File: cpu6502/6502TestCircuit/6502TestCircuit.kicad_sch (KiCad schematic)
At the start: 15 parts, among them J1 Power, J2 Power, J5 Ext RST, SW1 Reset, U6 L7805, U9 DS1813

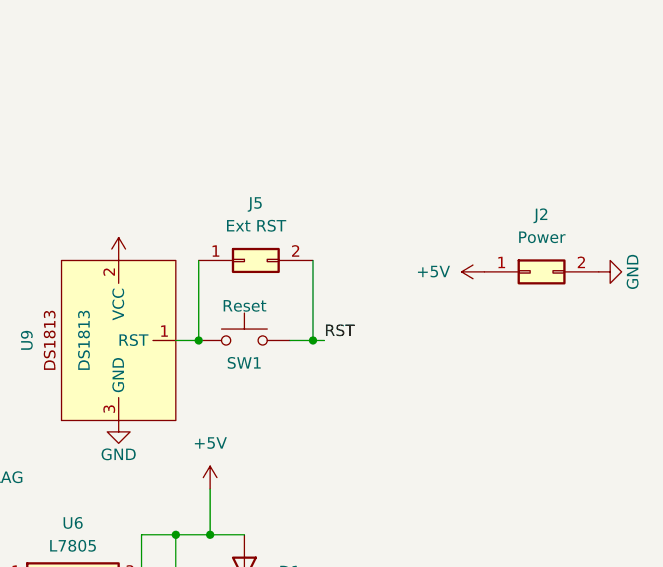
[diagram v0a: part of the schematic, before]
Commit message: PCB: Add RS232 RCV LED, get pours connected, CODE: checkpoint
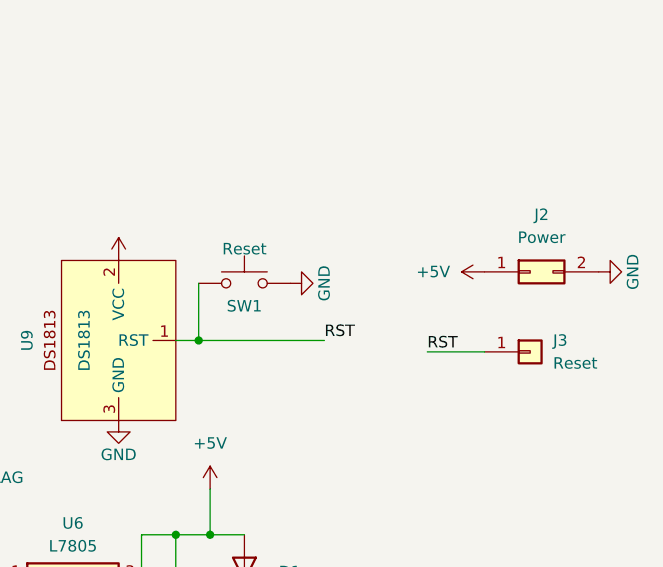
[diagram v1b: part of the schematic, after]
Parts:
- removed J5: Ext RST, Connector_PinHeader_2.54mm:PinHeader_2x01_P2.54mm_Vertical, symbol Connector_Generic:Conn_02x01
- added J3: Reset, Connector_PinHeader_2.54mm:PinHeader_1x01_P2.54mm_Vertical, symbol Connector_Generic:Conn_01x01
- U6: footprint Package_TO_SOT_THT:TO-220F-3_Horizontal_TabUp -> Package_TO_SOT_THT:TO-220-3_Horizontal_TabDown
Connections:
- net GND: now also SW1.2
- net RST: now also SW1.1, U9.1 (RST), J3.1 (Pin_1); no longer SW1.2
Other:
- moved on the sheet: SW1
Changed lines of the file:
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@@
 (kicad_sch (version 20230121) (generator eeschema)
   (paper "A4")
-  (junction (at 158.75 74.93) (diameter 0) (color 0 0 0 0)
-  )
   (junction (at 146.05 74.93) (diameter 0) (color 0 0 0 0)
   )
@@
     (stroke (width 0) (type default))
   )
+  (wire (pts (xy 171.45 76.2) (xy 177.8 76.2))
+    (stroke (width 0) (type default))
+  )
   (wire (pts (xy 120.65 101.6) (xy 121.92 101.6))
     (stroke (width 0) (type default))
   )
-  (wire (pts (xy 146.05 66.04) (xy 146.05 74.93))
-    (stroke (width 0) (type default))
-  )
   (wire (pts (xy 151.13 104.14) (xy 151.13 107.95))
     (stroke (width 0) (type default))
@@
     (stroke (width 0) (type default))
   )
+  (wire (pts (xy 143.51 74.93) (xy 146.05 74.93))
+    (stroke (width 0) (type default))
+  )
   (wire (pts (xy 147.32 96.52) (xy 151.13 96.52))
     (stroke (width 0) (type default))
@@
     (stroke (width 0) (type default))
   )
-  (wire (pts (xy 158.75 74.93) (xy 158.75 66.04))
+  (wire (pts (xy 146.05 74.93) (xy 160.02 74.93))
     (stroke (width 0) (type default))
   )
@@
     (stroke (width 0) (type default))
   )
-  (wire (pts (xy 156.21 74.93) (xy 158.75 74.93))
-    (stroke (width 0) (type default))
-  )
-  (wire (pts (xy 143.51 74.93) (xy 146.05 74.93))
-    (stroke (width 0) (type default))
-  )
   (wire (pts (xy 109.22 101.6) (xy 113.03 101.6))
     (stroke (width 0) (type default))
   )
+  (wire (pts (xy 146.05 68.58) (xy 146.05 74.93))
+    (stroke (width 0) (type default))
+  )
   (wire (pts (xy 121.92 101.6) (xy 121.92 107.95))
-    (stroke (width 0) (type default))
-  )
-  (wire (pts (xy 158.75 74.93) (xy 160.02 74.93))
     (stroke (width 0) (type default))
   )
@@
     (effects (font (size 1.27 1.27)) (justify left bottom))
   )
+  (label "RST" (at 171.45 76.2 0) (fields_autoplaced)
+    (effects (font (size 1.27 1.27)) (justify left bottom))
+  )
   (symbol (lib_id "power:+5V") (at 177.8 67.31 90) (unit 1)
     (in_bom yes) (on_board yes) (dnp no) (fields_autoplaced)
@@
     )
   )
-  (symbol (lib_id "Switch:SW_Push") (at 151.13 74.93 0) (unit 1)
-    (in_bom yes) (on_board yes) (dnp no)
-    (property "Reference" "SW1" (at 151.13 77.47 0)
-      (effects (font (size 1.27 1.27)))
-    )
-    (property "Value" "Reset" (at 151.13 71.12 0)
-      (effects (font (size 1.27 1.27)))
-    )
-    (property "Footprint" "Button_Switch_THT:SW_TH_Tactile_Omron_B3F-10xx" (at 151.13 69.85 0)
-      (effects (font (size 1.27 1.27)) hide)
-    )
-    (property "Datasheet" "~" (at 151.13 69.85 0)
+  (symbol (lib_id "Switch:SW_Push") (at 151.13 68.58 0) (unit 1)
+    (in_bom yes) (on_board yes) (dnp no)
+    (property "Reference" "SW1" (at 151.13 71.12 0)
+      (effects (font (size 1.27 1.27)))
+    )
+    (property "Value" "Reset" (at 151.13 64.77 0)
+      (effects (font (size 1.27 1.27)))
+    )
+    (property "Footprint" "Button_Switch_THT:SW_TH_Tactile_Omron_B3F-10xx" (at 151.13 63.5 0)
+      (effects (font (size 1.27 1.27)) hide)
+    )
+    (property "Datasheet" "~" (at 151.13 63.5 0)
       (effects (font (size 1.27 1.27)) hide)
     )
@@
       (effects (font (size 1.27 1.27)))
     )
-    (property "Footprint" "Package_TO_SOT_THT:TO-220F-3_Horizontal_TabUp" (at 132.715 105.41 0)
+    (property "Footprint" "Package_TO_SOT_THT:TO-220-3_Horizontal_TabDown" (at 132.715 105.41 0)
       (effects (font (size 1.27 1.27) italic) (justify left) hide)
     )
@@
     )
   )
+  (symbol (lib_id "power:GND") (at 156.21 68.58 90) (unit 1)
+    (in_bom yes) (on_board yes) (dnp no)
+    (property "Reference" "#PWR026" (at 162.56 68.58 0)
+      (effects (font (size 1.27 1.27)) hide)
+    )
+    (property "Value" "GND" (at 160.02 68.58 0)
+      (effects (font (size 1.27 1.27)))
+    )
+    (property "Footprint" "" (at 156.21 68.58 0)
+      (effects (font (size 1.27 1.27)) hide)
+    )
+    (property "Datasheet" "" (at 156.21 68.58 0)
+      (effects (font (size 1.27 1.27)) hide)
+    )
+    (pin "1")
+    (instances
+      (project "pcb6502"
+        (path "/aae31785-fe90-4323-8d48-945b25f108ea"
+          (reference "#PWR026") (unit 1)
+        )
+      )
+      (project "6502TestCircuit"
+        (path "/de11ec59-3146-4306-be5d-32ea1072df33"
+          (reference "#PWR03") (unit 1)
+        )
+      )
+    )
+  )
   (symbol (lib_id "Device:LED") (at 151.13 100.33 90) (unit 1)
     (in_bom yes) (on_board yes) (dnp no) (fields_autoplaced)
@@
     )
   )
+  (symbol (lib_id "Connector_Generic:Conn_01x01") (at 182.88 76.2 0) (unit 1)
+    (in_bom yes) (on_board yes) (dnp no) (fields_autoplaced)
+    (property "Reference" "J3" (at 185.42 74.93 0)
+      (effects (font (size 1.27 1.27)) (justify left))
+    )
+    (property "Value" "Reset" (at 185.42 77.47 0)
+      (effects (font (size 1.27 1.27)) (justify left))
+    )
+    (property "Footprint" "Connector_PinHeader_2.54mm:PinHeader_1x01_P2.54mm_Vertical" (at 182.88 76.2 0)
+      (effects (font (size 1.27 1.27)) hide)
+    )
+    (property "Datasheet" "~" (at 182.88 76.2 0)
+      (effects (font (size 1.27 1.27)) hide)
+    )
+    (pin "1")
+    (instances
+      (project "6502TestCircuit"
+        (path "/de11ec59-3146-4306-be5d-32ea1072df33"
+          (reference "J3") (unit 1)
+        )
+      )
+    )
+  )
   (symbol (lib_id "power:PWR_FLAG") (at 121.92 95.25 0) (unit 1)
     (in_bom yes) (on_board yes) (dnp no) (fields_autoplaced)
@@
         )
       )
-    )
-  )
-  (symbol (lib_id "Connector_Generic:Conn_02x01") (at 151.13 66.04 0) (unit 1)
-    (in_bom yes) (on_board yes) (dnp no) (fields_autoplaced)
-    (property "Reference" "J5" (at 152.4 59.69 0)
-      (effects (font (size 1.27 1.27)))
-    )
-    (property "Value" "Ext RST" (at 152.4 62.23 0)
-      (effects (font (size 1.27 1.27)))
-    )
-    (property "Footprint" "Connector_PinHeader_2.54mm:PinHeader_2x01_P2.54mm_Vertical" (at 151.13 66.04 0)
-      (effects (font (size 1.27 1.27)) hide)
-    )
-    (property "Datasheet" "~" (at 151.13 66.04 0)
-      (effects (font (size 1.27 1.27)) hide)
-    )
-    (pin "1")
-    (pin "2")
-    (instances
-      (project "pcb6502"
-        (path "/aae31785-fe90-4323-8d48-945b25f108ea"
-          (reference "J5") (unit 1)
-        )
-      )
-      (project "6502TestCircuit"
-        (path "/de11ec59-3146-4306-be5d-32ea1072df33"
-          (reference "J5") (unit 1)
-        )
-      )

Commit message: code changes (wip), set test PCB 2.0 to PCBway
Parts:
- removed J2: Power, Connector_PinHeader_2.54mm:PinHeader_2x01_P2.54mm_Vertical, symbol Connector_Generic:Conn_02x01
- removed J3: Reset, Connector_PinHeader_2.54mm:PinHeader_1x01_P2.54mm_Vertical, symbol Connector_Generic:Conn_01x01
- added C2, C3, C4, C5: 1uf, Capacitor_THT:C_Disc_D3.0mm_W1.6mm_P2.50mm, symbol Device:C
- added C6: 20pf, Capacitor_THT:C_Disc_D3.0mm_W1.6mm_P2.50mm, symbol Device:C
- added D2: SB140, Diode_THT:D_DO-41_SOD81_P10.16mm_Horizontal, symbol Diode:SB140
- added D4: Rec, LED_THT:LED_D3.0mm, symbol Device:LED
- added J1: CPU, Connector_PinHeader_2.54mm:PinHeader_1x19_P2.54mm_Vertical, symbol Connector_Generic:Conn_01x19
- added J2: IRQ, Connector_PinHeader_2.54mm:PinHeader_1x01_P2.54mm_Vertical, symbol Connector_Generic:Conn_01x01
- added J3: LCD, Connector_PinHeader_2.54mm:PinHeader_1x16_P2.54mm_Vertical, symbol Connector_Generic:Conn_01x16
- added J5: RS232, TerminalBlock_TE-Connectivity:TerminalBlock_TE_282834-3_1x03_P2.54mm_Horizontal, symbol Connector_Generic:Conn_01x03
- added R1: 220, Resistor_THT:R_Axial_DIN0207_L6.3mm_D2.5mm_P2.54mm_Vertical, symbol Device:R
- added R4: 1M, Resistor_THT:R_Axial_DIN0204_L3.6mm_D1.6mm_P7.62mm_Horizontal, symbol Device:R
- added R5: 1K, Resistor_THT:R_Axial_DIN0204_L3.6mm_D1.6mm_P2.54mm_Vertical, symbol Device:R
- added RV1: Contrast (10K), Potentiometer_THT:Potentiometer_Bourns_3386P_Vertical, symbol Device:R_Potentiometer_US
- added SW3: Debug, Button_Switch_THT:SW_TH_Tactile_Omron_B3F-10xx, symbol Switch:SW_Push
- added SW4: IRQ, Button_Switch_THT:SW_DIP_SPSTx03_Slide_6.7x9.18mm_W7.62mm_P2.54mm_LowProfile, symbol Switch:SW_DIP_x03
- added U4: 6522 (VIA), Package_DIP:DIP-40_W15.24mm_Socket, symbol PCM_65xx-library:W65C22NxP
- added U7: 6551 (ACIA), Package_DIP:DIP-28_W15.24mm_Socket, symbol PCM_65xx-library:W65C51NxP
- added U8: MAX232, Package_DIP:DIP-16_W7.62mm_Socket, symbol Interface_UART:MAX232
- added Y1: 1.8432 Mhz, Crystal:Crystal_HC49-4H_Vertical, symbol Device:Crystal
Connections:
- net +5V: now also J3.15 (Pin_15), J3.2 (Pin_2), R5.1, SW4.6, U4.20 (VCC), U7.15 (VCC), U8.16 (VCC)
- net GND: now also C4.1, C5.2, C6.2, J1.19 (Pin_19), J3.1 (Pin_1), J3.16 (Pin_16), J5.3 (Pin_3), R1.2, RV1.1, SW3.1, U4.1 (VSS), U7.1 (VSS), U8.15 (GND)
- net RST: now also J1.9 (Pin_9), U4.34 (~{RES}), U7.4 (~{RES})
- new net: D4.1 (K), R1.1
- new net: D2.1 (K), U7.26 (~{IRQ})
- new net: J3.3 (Pin_3), RV1.2
- new net: J5.1 (Pin_1), U8.14 (T1OUT)
- new net: D4.2 (A), J5.2 (Pin_2), U8.13 (R1IN)
- new net: C2.1, U8.1 (C1+)
- new net: C2.2, U8.3 (C1-)
- new net: C3.1, U8.4 (C2+)
- new net: C3.2, U8.5 (C2-)
- new net 232_VS+: C4.2, U8.2 (VS+)
- new net 232_VS-: C5.1, U8.6 (VS-)
- new net A0: J1.11 (Pin_11), U4.38 (RS0), U7.13 (RS0)
- new net A1: J1.12 (Pin_12), U4.37 (RS1), U7.14 (RS1)
- new net A12: J1.15 (Pin_15), U7.2 (CS1)
- new net A13: J1.16 (Pin_16), U4.24 (CS1)
- new net A2: J1.13 (Pin_13), U4.36 (RS2)
- new net A3: J1.14 (Pin_14), U4.35 (RS3)
- new net ACIAIRQ: D2.2 (A), SW4.5
- new net CA1: R5.2, SW3.2, U4.40 (CA1)
- new net CS2: J1.17 (Pin_17), U4.23 (~{CS2}), U7.3 (~{CS2})
- new net D0: J1.1 (Pin_1), U4.33 (D0), U7.18 (D0)
- new net D1: J1.2 (Pin_2), U4.32 (D1), U7.19 (D1)
- new net D2: J1.3 (Pin_3), U4.31 (D2), U7.20 (D2)
- new net D3: J1.4 (Pin_4), U4.30 (D3), U7.21 (D3)
- new net D4: J1.5 (Pin_5), U4.29 (D4), U7.22 (D4)
- new net D5: J1.6 (Pin_6), U4.28 (D5), U7.23 (D5)
- new net D6: J1.7 (Pin_7), U4.27 (D6), U7.24 (D6)
- new net D7: J1.8 (Pin_8), U4.26 (D7), U7.25 (D7)
- new net IRQ: J2.1 (Pin_1), SW4.1, SW4.2, SW4.3
- new net PA5: J3.4 (Pin_4), U4.7 (PA5)
- new net PA6: J3.5 (Pin_5), U4.8 (PA6)
- new net PA7: J3.6 (Pin_6), U4.9 (PA7)
- new net PB0: J3.7 (Pin_7), U4.10 (PB0)
- new net PB1: J3.8 (Pin_8), U4.11 (PB1)
- new net PB2: J3.9 (Pin_9), U4.12 (PB2)
- new net PB3: J3.10 (Pin_10), U4.13 (PB3)
- new net PB4: J3.11 (Pin_11), U4.14 (PB4)
- new net PB5: J3.12 (Pin_12), U4.15 (PB5)
- new net PB6: J3.13 (Pin_13), U4.16 (PB6)
- new net PB7: J3.14 (Pin_14), U4.17 (PB7)
- new net PHI2: J1.18 (Pin_18), U4.25 (ϕ2), U7.27 (ϕ2)
- new net RxD: U7.12 (RxD), U8.12 (R1OUT)
- new net R/W: J1.10 (Pin_10), U4.22 (R/~{W}), U7.28 (R/~{W})
- new net TxD: U7.10 (TxD), U8.11 (T1IN)
- new net VIAIRQ: SW4.4, U4.21 (~{IRQ})
- new net XTAL2: C6.1, R4.1, U7.7 (XTAL2), Y1.1
- new net XTLA1: R4.2, U7.6 (XTAL1), Y1.2
- no-connect marks 0 -> 20

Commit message: checkpoint, most significantly OS works!!
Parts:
- removed J1: CPU, Connector_PinHeader_2.54mm:PinHeader_1x19_P2.54mm_Vertical, symbol Connector_Generic:Conn_01x19
- added J1: CPU, Connector_PinHeader_2.54mm:PinHeader_1x20_P2.54mm_Vertical, symbol Connector_Generic:Conn_01x20
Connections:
- net +5V: now also J1.20 (Pin_20)
- net A0: now also J1.11 (Pin_11)
- net A1: now also J1.12 (Pin_12)
- net A12: now also J1.15 (Pin_15)
- net A13: now also J1.16 (Pin_16)
- net A2: now also J1.13 (Pin_13)
- net A3: now also J1.14 (Pin_14)
- net CS2: now also J1.17 (Pin_17)
- net D0: now also J1.1 (Pin_1)
- net D1: now also J1.2 (Pin_2)
- net D2: now also J1.3 (Pin_3)
- net D3: now also J1.4 (Pin_4)
- net D4: now also J1.5 (Pin_5)
- net D5: now also J1.6 (Pin_6)
- net D6: now also J1.7 (Pin_7)
- net D7: now also J1.8 (Pin_8)
- net GND: now also J1.19 (Pin_19)
- net PHI2: now also J1.18 (Pin_18)
- net RST: now also J1.9 (Pin_9)
- net R/W: now also J1.10 (Pin_10)
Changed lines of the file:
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@@
+    (stroke (width 0) (type default))
+  )
+  (wire (pts (xy 128.27 80.01) (xy 133.35 80.01))
     (stroke (width 0) (type default))
   )
@@
     )
   )
-  (symbol (lib_id "power:GND") (at 133.35 80.01 0) (unit 1)
+  (symbol (lib_id "power:GND") (at 128.27 80.01 270) (unit 1)
     (in_bom yes) (on_board yes) (dnp no)
-    (property "Reference" "#PWR036" (at 133.35 86.36 0)
-      (effects (font (size 1.27 1.27)) hide)
-    )
-    (property "Value" "GND" (at 133.35 83.82 0)
-      (effects (font (size 1.27 1.27)))
-    )
-    (property "Footprint" "" (at 133.35 80.01 0)
-      (effects (font (size 1.27 1.27)) hide)
-    )
-    (property "Datasheet" "" (at 133.35 80.01 0)
+    (property "Reference" "#PWR036" (at 121.92 80.01 0)
+      (effects (font (size 1.27 1.27)) hide)
+    )
+    (property "Value" "GND" (at 124.46 80.01 0)
+      (effects (font (size 1.27 1.27)))
+    )
+    (property "Footprint" "" (at 128.27 80.01 0)
+      (effects (font (size 1.27 1.27)) hide)
+    )
+    (property "Datasheet" "" (at 128.27 80.01 0)
       (effects (font (size 1.27 1.27)) hide)
     )
@@
         (path "/de11ec59-3146-4306-be5d-32ea1072df33"
           (reference "#PWR03") (unit 1)
+        )
+      )
+    )
+  )
+  (symbol (lib_id "power:+5V") (at 133.35 82.55 90) (unit 1)
+    (in_bom yes) (on_board yes) (dnp no) (fields_autoplaced)
+    (property "Reference" "#PWR08" (at 137.16 82.55 0)
+      (effects (font (size 1.27 1.27)) hide)
+    )
+    (property "Value" "+5V" (at 129.54 82.55 90)
+      (effects (font (size 1.27 1.27)) (justify left))
+    )
+    (property "Footprint" "" (at 133.35 82.55 0)
+      (effects (font (size 1.27 1.27)) hide)
+    )
+    (property "Datasheet" "" (at 133.35 82.55 0)
+      (effects (font (size 1.27 1.27)) hide)
+    )
+    (pin "1")
+    (instances
+      (project "pcb6502"
+        (path "/aae31785-fe90-4323-8d48-945b25f108ea"
+          (reference "#PWR08") (unit 1)
+        )
+      )
+      (project "6502TestCircuit"
+        (path "/de11ec59-3146-4306-be5d-32ea1072df33"
+          (reference "#PWR09") (unit 1)
         )
       )
@@
     )
   )
-  (symbol (lib_id "Device:LED") (at 248.92 161.29 180) (unit 1)
-    (in_bom yes) (on_board yes) (dnp no)
-    (property "Reference" "D4" (at 246.38 157.48 0)
-      (effects (font (size 1.27 1.27)) (justify right))
-    )
-    (property "Value" "Rec" (at 247.65 163.83 0)
-      (effects (font (size 1.27 1.27)) (justify right))
-    )
-    (property "Footprint" "LED_THT:LED_D3.0mm" (at 248.92 161.29 0)
-      (effects (font (size 1.27 1.27)) hide)
-    )
-    (property "Datasheet" "~" (at 248.92 161.29 0)
-      (effects (font (size 1.27 1.27)) hide)
-    )
-    (pin "1")
-    (pin "2")
-    (instances
-      (project "pcb6502"
-        (path "/aae31785-fe90-4323-8d48-945b25f108ea"
-          (reference "D4") (unit 1)
-        )
-      )
-      (project "6502TestCircuit"
-        (path "/de11ec59-3146-4306-be5d-32ea1072df33"
-          (reference "D4") (unit 1)
-        )
-      )
-    )
-  )
-  (symbol (lib_id "Connector_Generic:Conn_01x19") (at 138.43 57.15 0) (unit 1)
-    (in_bom yes) (on_board yes) (dnp no) (fields_autoplaced)
-    (property "Reference" "J1" (at 140.97 55.88 0)
-      (effects (font (size 1.27 1.27)) (justify left))
-    )
-    (property "Value" "CPU" (at 140.97 58.42 0)
-      (effects (font (size 1.27 1.27)) (justify left))
-    )
-    (property "Footprint" "Connector_PinHeader_2.54mm:PinHeader_1x19_P2.54mm_Vertical" (at 138.43 57.15 0)
+  (symbol (lib_id "Connector_Generic:Conn_01x20") (at 138.43 57.15 0) (unit 1)
+    (in_bom yes) (on_board yes) (dnp no) (fields_autoplaced)
+    (property "Reference" "J1" (at 140.97 57.15 0)
+      (effects (font (size 1.27 1.27)) (justify left))
+    )
+    (property "Value" "CPU" (at 140.97 59.69 0)
+      (effects (font (size 1.27 1.27)) (justify left))
+    )
+    (property "Footprint" "Connector_PinHeader_2.54mm:PinHeader_1x20_P2.54mm_Vertical" (at 138.43 57.15 0)
       (effects (font (size 1.27 1.27)) hide)
     )
@@
     (pin "19")
     (pin "2")
+    (pin "20")
     (pin "3")
     (pin "4")
@@
         )
       )
+    )
+  )
+  (symbol (lib_id "Device:LED") (at 248.92 161.29 180) (unit 1)
+    (in_bom yes) (on_board yes) (dnp no)
+    (property "Reference" "D4" (at 246.38 157.48 0)
+      (effects (font (size 1.27 1.27)) (justify right))
+    )
+    (property "Value" "Rec" (at 247.65 163.83 0)
+      (effects (font (size 1.27 1.27)) (justify right))
+    )
+    (property "Footprint" "LED_THT:LED_D3.0mm" (at 248.92 161.29 0)
+      (effects (font (size 1.27 1.27)) hide)
+    )
+    (property "Datasheet" "~" (at 248.92 161.29 0)
+      (effects (font (size 1.27 1.27)) hide)
+    )
+    (pin "1")
+    (pin "2")
+    (instances
+      (project "pcb6502"
+        (path "/aae31785-fe90-4323-8d48-945b25f108ea"
+          (reference "D4") (unit 1)
+        )
+      )
+      (project "6502TestCircuit"
+        (path "/de11ec59-3146-4306-be5d-32ea1072df33"
+          (reference "D4") (unit 1)
+        )
+      )
